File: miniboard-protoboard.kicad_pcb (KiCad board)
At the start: 2 copper layers, 50.8 x 50.8 mm, 530 parts

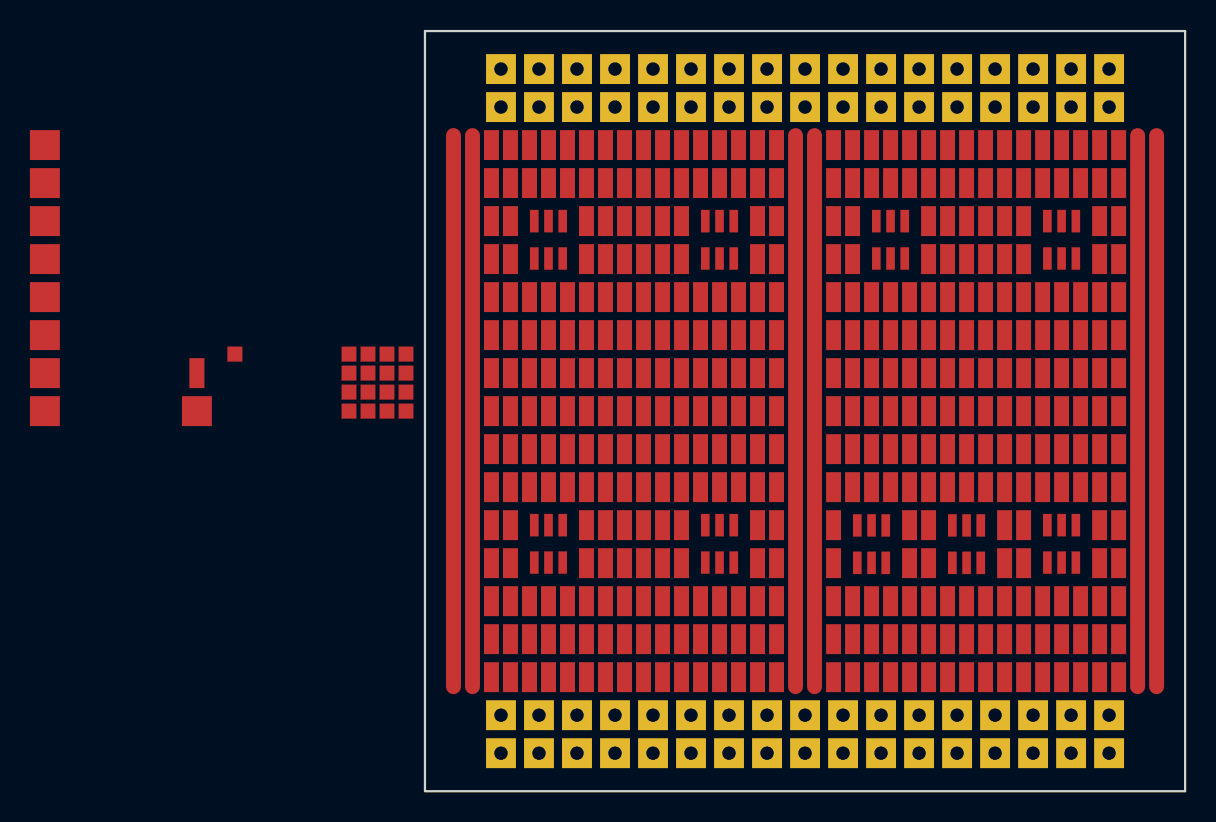
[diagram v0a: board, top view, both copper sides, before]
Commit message: Move pads in a more pleasing way. Generate gerbers and pdf
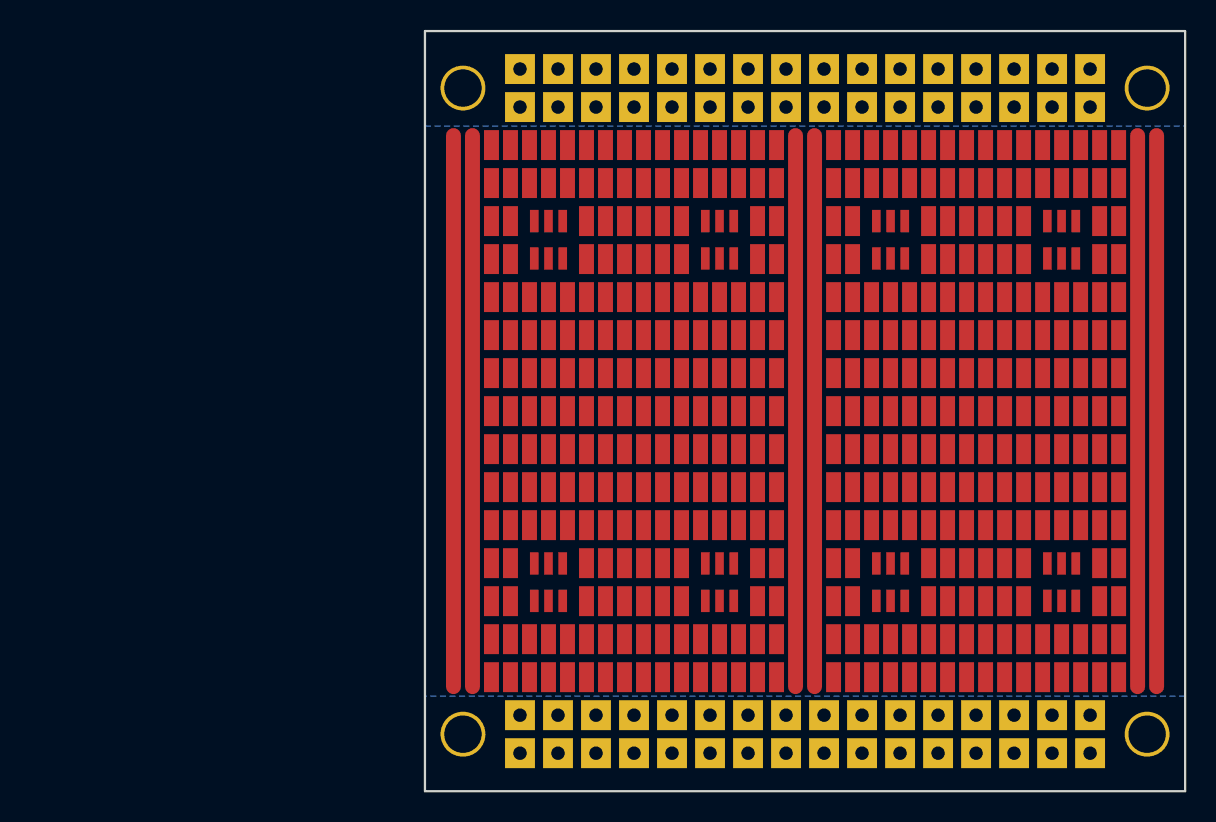
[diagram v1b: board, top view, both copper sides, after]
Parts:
- removed the Ref** at (147.3, 101.6)
- removed the Ref** at (147.3, 99.1)
- removed the Ref** at (147.3, 100.3)
- removed the Ref** at (147.3, 97.8)
- removed the Ref** at (148.6, 97.8)
- removed the Ref** at (148.6, 99.1)
- removed the Ref** at (148.6, 101.6)
- removed the Ref** at (148.6, 100.3)
- removed the Ref** at (149.9, 100.3)
- removed the Ref** at (149.9, 101.6)
- removed the Ref** at (149.9, 99.1)
- removed the Ref** at (149.9, 97.8)
- removed the Ref** at (151.1, 101.6)
- removed the Ref** at (151.1, 100.3)
- removed the Ref** at (151.1, 99.1)
- removed the Ref** at (151.1, 97.8)
- removed the Ref** at (139.7, 97.8)
- removed the Ref** at (137.2, 99.1)
- removed the proto_pad2 at (157.5, 121.9)
- removed the proto_pad2 at (157.5, 124.5)
- removed the proto_pad2 at (127.0, 88.9)
- removed the proto_pad2 at (127.0, 91.4)
- removed the proto_pad2 at (127.0, 83.8)
- removed the proto_pad2 at (127.0, 86.4)
- removed the proto_pad2 at (157.5, 81.3)
- removed the proto_pad2 at (157.5, 78.7)
- removed the proto_pad2 at (127.0, 94.0)
- removed the proto_pad2 at (127.0, 96.5)
- removed the proto_pad2 at (127.0, 99.1)
- removed the proto_pad2 at (127.0, 101.6)
- removed the proto_pad2 at (137.2, 101.6)
- removed the proto_sot23 at (188.6, 110.5)
- added Ref**: Val**, protolib:proto_pad4, F.Cu at (189.9, 109.2)
- added Ref**: Val**, protolib:proto_pad4, F.Cu at (189.9, 111.8)
- added Ref**: Val**, protolib:proto_pad4, F.Cu at (188.6, 111.8)
- added Ref**: Val**, protolib:proto_pad4, F.Cu at (188.6, 109.2)
- added Ref**: Val**, protolib:proto_pad4, F.Cu at (181.0, 111.8)
- added Ref**: Val**, protolib:proto_pad4, F.Cu at (181.0, 109.2)
- added hole_2.5mm: VAL**, mechanics:hole_2.5mm, F.Cu at (154.9, 80.0)
- added hole_2.5mm: VAL**, mechanics:hole_2.5mm, F.Cu at (154.9, 123.2)
- added hole_2.5mm: VAL**, mechanics:hole_2.5mm, F.Cu at (200.7, 123.2)
- added hole_2.5mm: VAL**, mechanics:hole_2.5mm, F.Cu at (200.7, 80.0)
- moved Ref** 12.5 mm to (170.8, 109.2)
- moved Ref** 12.5 mm to (173.4, 109.2)
- moved Ref** 12.5 mm to (184.8, 109.2)
- moved Ref** 12.5 mm to (182.2, 109.2)
- moved Ref** 12.5 mm to (172.1, 109.2)
- moved Ref** 12.5 mm to (183.5, 109.2)
- moved Ref** 5.08 mm to (193.7, 109.2)
- moved Ref** 5.08 mm to (159.4, 109.2)
- moved Ref** 5.08 mm to (160.7, 109.2)
- moved Ref** 5.08 mm to (161.9, 109.2)
- moved Ref** 5.08 mm to (194.9, 109.2)
- moved Ref** 5.08 mm to (196.2, 109.2)
- moved proto_sot23 2.84 mm to (183.5, 113.0)
- moved proto_sot23 2.56 mm to (194.9, 113.0)
- moved proto_sot23 2.56 mm to (172.1, 113.0)
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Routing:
- added copper zone on B.Cu, net (none)
